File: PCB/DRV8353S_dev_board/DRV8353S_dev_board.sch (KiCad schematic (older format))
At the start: 136 parts

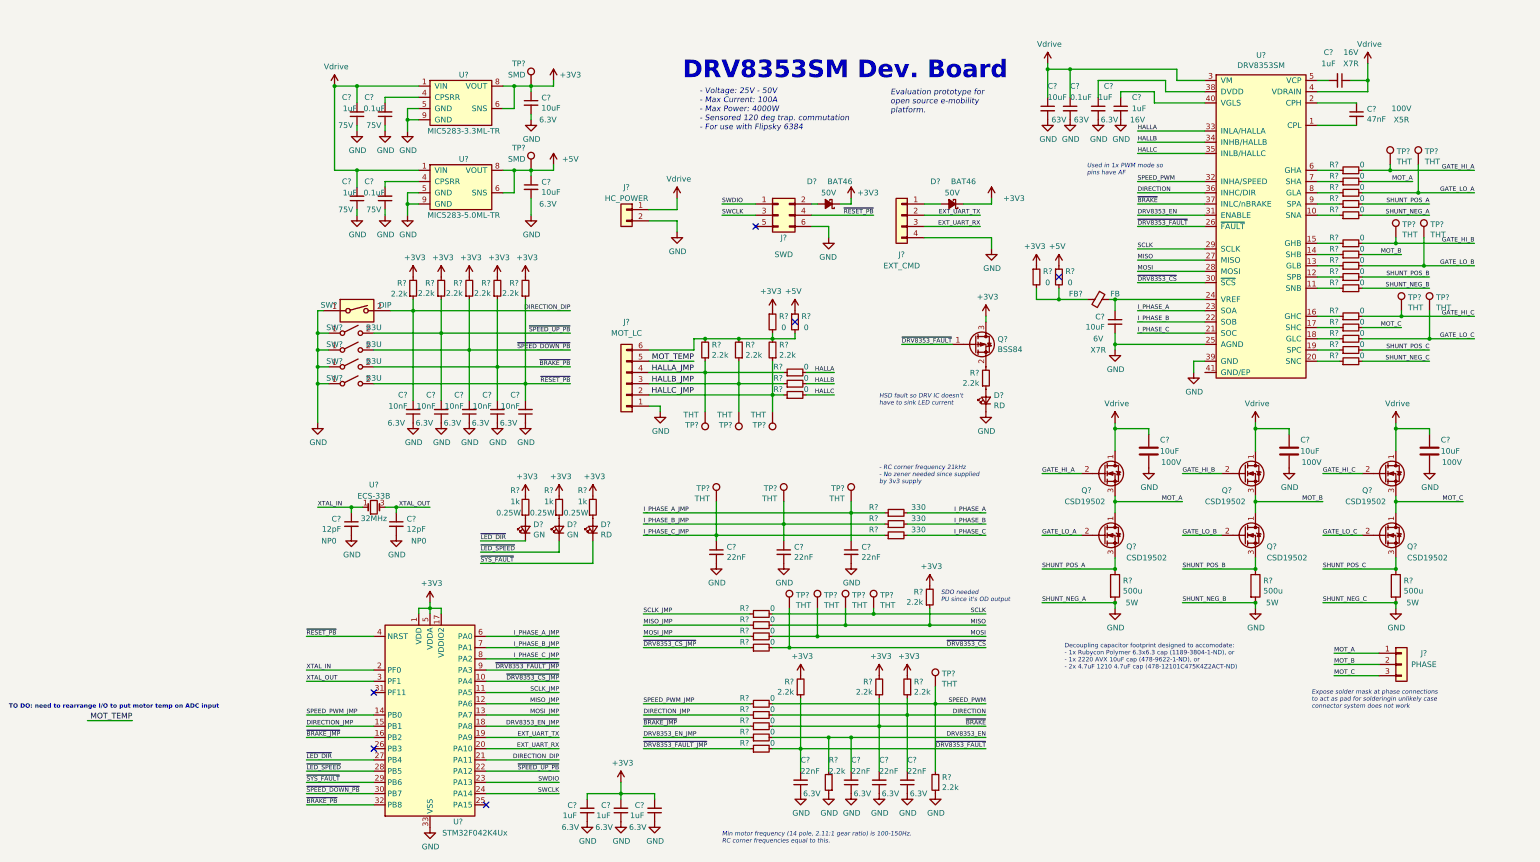
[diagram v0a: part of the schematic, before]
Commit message: High Current Routing planning
Planning how the high current routing will work with the gate drive signals
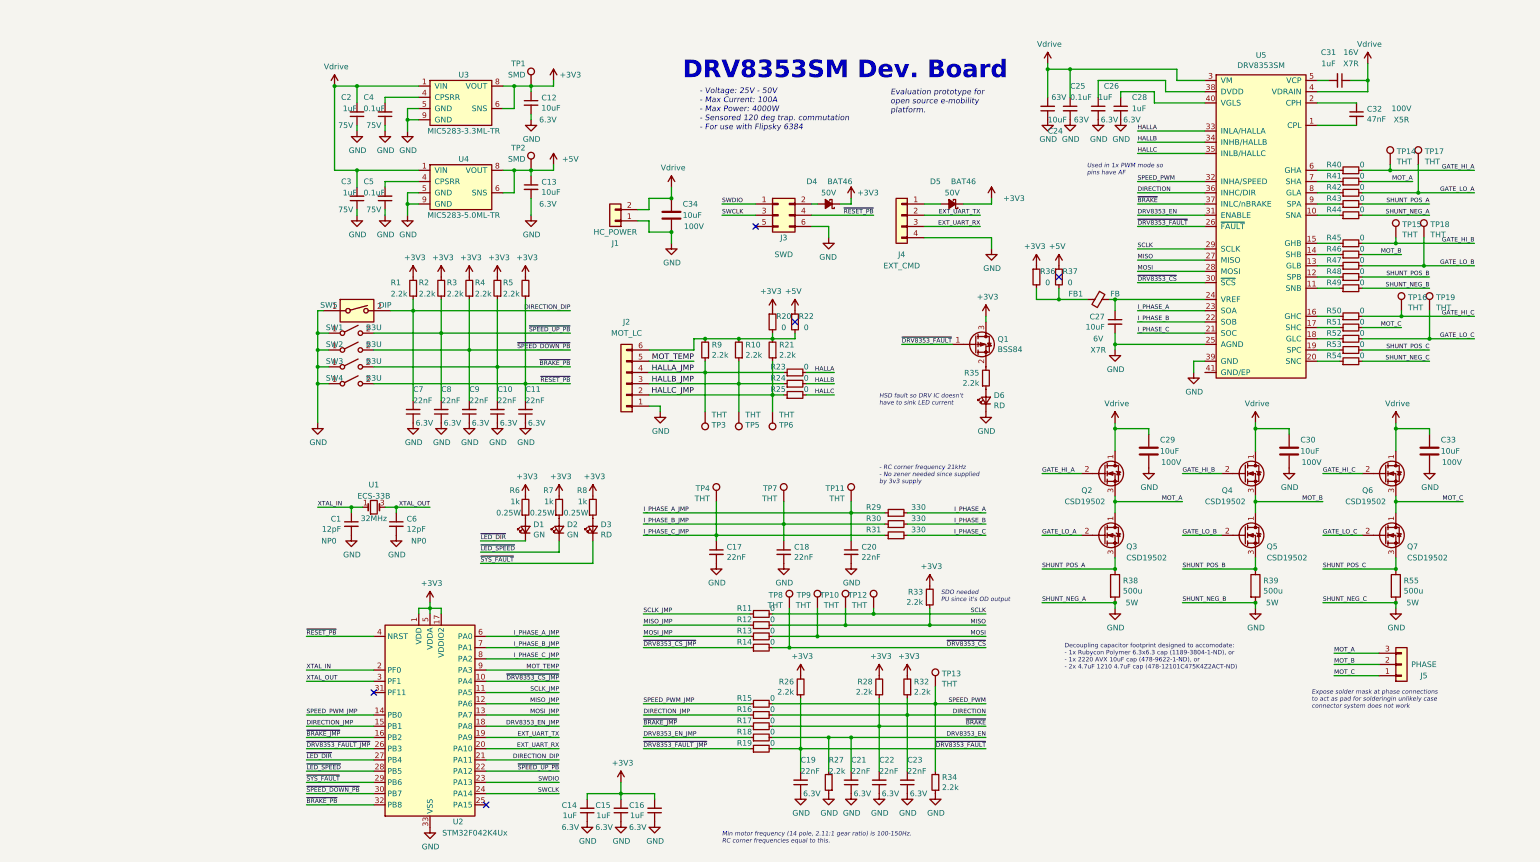
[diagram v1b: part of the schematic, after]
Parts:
- removed C? (x2): 1uF, symbol Device:C_Small
- removed C? (x5): 10nF, symbol Device:C_Small
- removed C? (x2): 1uF, Capacitor_SMD:C_0603_1608Metric, symbol Device:C_Small
- removed R? (x5): 2.2k, symbol Device:R_Small
- removed TP? (x16): THT, TestPoint:TestPoint_Keystone_5000-5004_Miniature, symbol Connector:TestPoint
- added C10, C11, C7, C8, C9: 22nF, Capacitor_SMD:C_0603_1608Metric, symbol Device:C_Small
- added C15, C16, C28, C3: 1uF, Capacitor_SMD:C_0805_2012Metric, symbol Device:C_Small
- added C34: 10uF, DRV8353S_dev_board:bridge_caps, symbol Device:C
- added R1, R2, R3, R4, R5: 2.2k, Resistor_SMD:R_0603_1608Metric, symbol Device:R_Small
- added TP10, TP11, TP12, TP13, TP14, TP15, TP16, TP17, TP18, TP19, TP3, TP5, TP6, TP7, TP8, TP9: THT, DRV8353S_dev_board:keystone_5001, symbol Connector:TestPoint
- C1, C6: renamed from C?; footprint (none) -> Capacitor_SMD:C_0603_1608Metric; Digikey (none) -> 478-10188-1-ND
- C12, C13, C24, C27: renamed from C?; footprint (none) -> Capacitor_SMD:C_1210_3225Metric; Digikey (none) -> 445-181609-1-ND
- C14: renamed from C?; footprint Capacitor_SMD:C_0603_1608Metric -> Capacitor_SMD:C_0805_2012Metric; Digikey (none) -> 478-12143-1-ND
- C17, C18, C19, C20, C21, C22, C23: renamed from C?; Digikey (none) -> 445-5663-1-ND
- C2, C26, C31: renamed from C?; footprint (none) -> Capacitor_SMD:C_0805_2012Metric; Digikey (none) -> 478-12143-1-ND
- C25, C4, C5: renamed from C?; footprint (none) -> Capacitor_SMD:C_0805_2012Metric; Digikey (none) -> 1276-6840-1-ND
- C32: renamed from C?; footprint (none) -> Capacitor_SMD:C_0603_1608Metric; Digikey (none) -> 311-4050-1-ND
- TP4: renamed from TP?; footprint TestPoint:TestPoint_Keystone_5000-5004_Miniature -> DRV8353S_dev_board:keystone_5001
- gave numbers to parts that had none: 84
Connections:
- net +3V3: now also C15.2, C16.2, R1.2, R2.2, R3.2, R4.2, R5.2
- net DIRECTION_DIP: now also C7.2, R1.1
- net GATE_HI_A: now also TP14.1
- net GATE_HI_B: now also TP15.1
- net GATE_HI_C: now also TP16.1
- net GATE_LO_A: now also TP17.1
- net GATE_LO_B: now also TP18.1
- net GATE_LO_C: now also TP19.1
- net GND: now also C24.1, J1.1 (Pin_1), C10.1, C11.1, C15.1, C16.1, C28.2, C3.1, C34.2, C7.1, C8.1, C9.1; no longer C24.2, J1.2 (Pin_2)
- net HALLA_JMP: now also TP3.1
- net HALLB_JMP: now also TP5.1
- net HALLC_JMP: now also TP6.1
- net I_PHASE_A_JMP: now also TP11.1
- net I_PHASE_B_JMP: now also TP7.1
- net MISO: now also TP10.1
- net MOSI: now also TP9.1
- net MOT_A: now also J5.3 (Pin_3); no longer J5.1 (Pin_1)
- net MOT_C: now also J5.1 (Pin_1); no longer J5.3 (Pin_3)
- net MOT_TEMP: now also U2.9 (PA3)
- net SCLK: now also TP12.1
- net SPEED_PWM: now also TP13.1
- net Vdrive: now also C24.2, J1.2 (Pin_2), C3.2, C34.1; no longer C24.1, J1.1 (Pin_1)
- net ~BRAKE_PB: now also C10.2, R4.1
- net ~DRV8353_CS: now also TP8.1
- net ~DRV8353_FAULT_JMP: now also U2.26 (PB3); no longer U2.9 (PA3)
- net ~RESET_PB: now also C11.2, R5.1
- net ~SPEED_DOWN_PB: now also C9.2, R3.1
- net ~SPEED_UP_PB: now also C8.2, R2.1
- net at U5.40 (VGLS): now also C28.1
- no-connect marks 6 -> 5
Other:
- note removed: "TO DO: need to rearrange I/O to put motor temp on ADC input"
- moved on the sheet: J1

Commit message: more routing work
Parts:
- added C35: 22nF, Capacitor_SMD:C_0603_1608Metric, symbol Device:C_Small
- added R56: 330, Resistor_SMD:R_0603_1608Metric, symbol Device:R_Small
- added TP20: THT, DRV8353S_dev_board:keystone_5001, symbol Connector:TestPoint
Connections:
- net GND: now also C35.2
- net HALLA: now also R9.1, TP3.1
- net HALLA_JMP: no longer R9.1, TP3.1
- net HALLB: now also R10.1, TP5.1
- net HALLB_JMP: no longer R10.1, TP5.1
- net HALLC: now also R21.1, TP6.1
- net HALLC_JMP: no longer R21.1, TP6.1
- net I_PHASE_A_JMP: now also U2.9 (PA3); no longer U2.6 (PA0)
- net I_PHASE_B_JMP: now also U2.8 (PA2); no longer U2.7 (PA1)
- net I_PHASE_C_JMP: now also U2.7 (PA1); no longer U2.8 (PA2)
- net MOT_TEMP: now also R56.2; no longer U2.9 (PA3)
- new net MOT_TEMP_JMP: C35.1, R56.1, TP20.1, U2.6 (PA0)
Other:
- moved on the sheet: C17, C18, C20, R10, R20, R21, R22, R23, R24, R25, R29, R30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

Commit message: Final (?) layout
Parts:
- removed R36, R37: 0, Resistor_SMD:R_0603_1608Metric, symbol Device:R_Small
- C1, C10, C11, C12, C13, C14, C15, C16, C17, C18, C19, C2, C20, C21, C22, C23, C24, C25, C26, C27, C28, C3, C31, C32, C35, C4, C5, C6, C7, C8, C9: symbol Device:C_Small -> DRV8353S_dev_board-rescue:C_Small-Device
- C29, C30, C33, C34: symbol Device:C -> DRV8353S_dev_board-rescue:C-Device
- D1, D2, D3, D6: symbol Device:LED_Small -> DRV8353S_dev_board-rescue:LED_Small-Device
- D4, D5: symbol Device:D_Schottky_Small_ALT -> DRV8353S_dev_board-rescue:D_Schottky_Small_ALT-Device
- FB1: symbol Device:Ferrite_Bead_Small -> DRV8353S_dev_board-rescue:Ferrite_Bead_Small-Device
- J1: symbol Connector_Generic:Conn_01x02 -> DRV8353S_dev_board-rescue:Conn_01x02-Connector_Generic
- J2: symbol Connector_Generic:Conn_01x06 -> DRV8353S_dev_board-rescue:Conn_01x06-Connector_Generic
- J3: symbol Connector_Generic:Conn_02x03_Odd_Even -> DRV8353S_dev_board-rescue:Conn_02x03_Odd_Even-Connector_Generic
- J4: symbol Connector_Generic:Conn_01x04 -> DRV8353S_dev_board-rescue:Conn_01x04-Connector_Generic
- J5: symbol Connector_Generic:Conn_01x03 -> DRV8353S_dev_board-rescue:Conn_01x03-Connector_Generic
- Q1: symbol Device:Q_PMOS_GSD -> DRV8353S_dev_board-rescue:Q_PMOS_GSD-Device
- Q2, Q3, Q4, Q5, Q6, Q7: symbol Device:Q_NMOS_DGS -> DRV8353S_dev_board-rescue:Q_NMOS_DGS-Device
- R1, R10, R11, R12, R13, R14, R15, R16, R17, R18, R19, R2, R20, R21, R22, R23, R24, R25, R26, R27, R28, R29, R3, R30, R31, R32, R33, R34, R35, R4, R40, R41, R42, R43, R44, R45, R46, R47, R48, R49, R5, R50, R51, R52, R53, R54, R56, R6, R7, R8, R9: symbol Device:R_Small -> DRV8353S_dev_board-rescue:R_Small-Device
- R38, R39, R55: symbol Device:R -> DRV8353S_dev_board-rescue:R-Device
- SW1, SW2, SW3, SW4: symbol Switch:SW_SPST -> DRV8353S_dev_board-rescue:SW_SPST-Switch
- SW5: symbol Switch:SW_DIP_x01 -> DRV8353S_dev_board-rescue:SW_DIP_x01-Switch
- TP1, TP10, TP11, TP12, TP13, TP14, TP15, TP16, TP17, TP18, TP19, TP2, TP20, TP3, TP4, TP5, TP6, TP7, TP8, TP9: symbol Connector:TestPoint -> DRV8353S_dev_board-rescue:TestPoint-Connector
- U2: symbol MCU_ST_STM32F0:STM32F042K4Ux -> DRV8353S_dev_board-rescue:STM32F042K4Ux-MCU_ST_STM32F0
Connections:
- net DIRECTION_DIP: now also U2.29 (PB6); no longer U2.21 (PA11)
- net DIRECTION_JMP: now also U2.16 (PB2); no longer U2.15 (PB1)
- net DRV8353_EN_JMP: now also U2.15 (PB1); no longer U2.18 (PA8)
- net GND: now also J3.2 (Pin_2), U5.41 (GND/EP); no longer J3.6 (Pin_6)
- net I_PHASE_A_JMP: now also U2.8 (PA2); no longer U2.9 (PA3)
- net I_PHASE_B_JMP: now also U2.7 (PA1); no longer U2.8 (PA2)
- net I_PHASE_C_JMP: now also U2.6 (PA0); no longer U2.7 (PA1)
- net MOT_TEMP: now also TP20.1
- net MOT_TEMP_JMP: now also U2.9 (PA3); no longer TP20.1, U2.6 (PA0)
- net SPEED_PWM_JMP: now also U2.32 (PB8); no longer U2.14 (PB0)
- net ~BRAKE_JMP: now also U2.18 (PA8); no longer U2.16 (PB2)
- net ~BRAKE_PB: now also U2.26 (PB3); no longer U2.32 (PB8)
- net ~DRV8353_FAULT_JMP: now also U2.14 (PB0); no longer U2.26 (PB3)
- net ~LED_DIR: now also U2.25 (PA15); no longer U2.27 (PB4)
- net ~LED_SPEED: now also U2.22 (PA12); no longer U2.28 (PB5)
- net ~RESET_PB: now also J3.6 (Pin_6); no longer J3.4 (Pin_4)
- net ~SPEED_DOWN_PB: now also U2.27 (PB4); no longer U2.30 (PB7)
- net ~SPEED_UP_PB: now also U2.28 (PB5); no longer U2.22 (PA12)
- net ~SYS_FAULT: now also U2.21 (PA11); no longer U2.29 (PB6)
- net at D4.2 (A): now also J3.5 (Pin_5); no longer J3.2 (Pin_2)
- no-connect marks 5 -> 4
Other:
- moved on the sheet: C14, C15, C16, TP20

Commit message: Final Routing
Moved around encoder stuff. Also added decoupling capacitor near encoder connector.
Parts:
- added C36: 22nF, Capacitor_SMD:C_0603_1608Metric, symbol DRV8353S_dev_board-rescue:C_Small-Device
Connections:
- net GND: now also C36.2
- net HALLA: no longer R9.1
- net HALLA_JMP: now also R9.1
- net HALLB: no longer R10.1
- net HALLB_JMP: now also R10.1
- net HALLC: no longer R21.1
- net HALLC_JMP: now also R21.1
- net at J2.6 (Pin_6), R10.2, R20.2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: now also C36.1
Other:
- moved on the sheet: J2, R10, R20, R21, R22, R23, R24, R25, R9, TP3, TP5, TP6

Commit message: Most DRV routing done.
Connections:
- net I_PHASE_A: now also TP11.1
- net I_PHASE_A_JMP: no longer TP11.1
- net I_PHASE_B: now also TP7.1
- net I_PHASE_B_JMP: no longer TP7.1
- net I_PHASE_C: now also TP4.1
- net I_PHASE_C_JMP: no longer TP4.1
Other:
- moved on the sheet: R29, R30, R31, R56, TP11, TP20, TP4, TP7
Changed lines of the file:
@@
 	1    0    0    -1
 $EndComp
-Text Notes 5200 4450 0    39   Italic 0
+Text Notes 4350 4400 0    39   Italic 0
 - RC corner frequency 21kHz \n- No zener needed since supplied\nby 3v3 supply
 $Comp
 L DRV8353S_dev_board-rescue:R_Small-Device R56
 U 1 1 6071FAF6
-P 5950 4550
-F 0 "R56" V 6000 4750 50  0000 C CNN
-F 1 "330" V 6000 4350 50  0000 C CNN
-F 2 "Resistor_SMD:R_0603_1608Metric" H 5950 4550 50  0001 C CNN
-F 3 "https://www.bourns.com/docs/product-datasheets/CRxxxxx.pdf" H 5950 4550 50  0001 C CNN
-F 4 "CR0603-JW-331ELFCT-ND" V 5950 4550 50  0001 C CNN "Digikey"
-	1    5950 4550
+P 5650 4550
+F 0 "R56" V 5700 4750 50  0000 C CNN
+F 1 "330" V 5700 4350 50  0000 C CNN
+F 2 "Resistor_SMD:R_0603_1608Metric" H 5650 4550 50  0001 C CNN
+F 3 "https://www.bourns.com/docs/product-datasheets/CRxxxxx.pdf" H 5650 4550 50  0001 C CNN
+F 4 "CR0603-JW-331ELFCT-ND" V 5650 4550 50  0001 C CNN "Digikey"
+	1    5650 4550
 	0    -1   -1   0
 $EndComp
@@
 L DRV8353S_dev_board-rescue:R_Small-Device R29
 U 1 1 6043F748
-P 5950 4650
-F 0 "R29" V 6000 4850 50  0000 C CNN
-F 1 "330" V 6000 4450 50  0000 C CNN
-F 2 "Resistor_SMD:R_0603_1608Metric" H 5950 4650 50  0001 C CNN
-F 3 "https://www.bourns.com/docs/product-datasheets/CRxxxxx.pdf" H 5950 4650 50  0001 C CNN
-F 4 "CR0603-JW-331ELFCT-ND" V 5950 4650 50  0001 C CNN "Digikey"
-	1    5950 4650
+P 5650 4650
+F 0 "R29" V 5700 4850 50  0000 C CNN
+F 1 "330" V 5700 4450 50  0000 C CNN
+F 2 "Resistor_SMD:R_0603_1608Metric" H 5650 4650 50  0001 C CNN
+F 3 "https://www.bourns.com/docs/product-datasheets/CRxxxxx.pdf" H 5650 4650 50  0001 C CNN
+F 4 "CR0603-JW-331ELFCT-ND" V 5650 4650 50  0001 C CNN "Digikey"
+	1    5650 4650
 	0    -1   -1   0
 $EndComp
 Wire Wire Line
-	6350 4550 6350 4450
+	6400 4550 6400 4450
 $Comp
 L DRV8353S_dev_board-rescue:TestPoint-Connector TP20
 U 1 1 608C7A2F
-P 6350 4450
-F 0 "TP20" H 6300 4750 50  0000 L CNN
-F 1 "THT" H 6300 4650 50  0000 L CNN
-F 2 "DRV8353S_dev_board:keystone_5001" H 6550 4450 50  0001 C CNN
-F 3 "https://www.keyelco.com/userAssets/file/M65p56.pdf" H 6550 4450 50  0001 C CNN
-F 4 "36-5001-ND" H 6350 4450 50  0001 C CNN "Digikey"
-	1    6350 4450
+P 6400 4450
+F 0 "TP20" H 6350 4750 50  0000 L CNN
+F 1 "THT" H 6350 4650 50  0000 L CNN
+F 2 "DRV8353S_dev_board:keystone_5001" H 6600 4450 50  0001 C CNN
+F 3 "https://www.keyelco.com/userAssets/file/M65p56.pdf" H 6600 4450 50  0001 C CNN
+F 4 "36-5001-ND" H 6400 4450 50  0001 C CNN "Digikey"
+	1    6400 4450
 	-1   0    0    -1
 $EndComp
@@
 L DRV8353S_dev_board-rescue:TestPoint-Connector TP11
 U 1 1 604F9F69
-P 5050 4450
-F 0 "TP11" H 5000 4750 50  0000 L CNN
-F 1 "THT" H 5000 4650 50  0000 L CNN
-F 2 "DRV8353S_dev_board:keystone_5001" H 5250 4450 50  0001 C CNN
-F 3 "https://www.keyelco.com/userAssets/file/M65p56.pdf" H 5250 4450 50  0001 C CNN
-F 4 "36-5001-ND" H 5050 4450 50  0001 C CNN "Digikey"
-	1    5050 4450
+P 6250 4450
+F 0 "TP11" H 6200 4750 50  0000 L CNN
+F 1 "THT" H 6200 4650 50  0000 L CNN
+F 2 "DRV8353S_dev_board:keystone_5001" H 6450 4450 50  0001 C CNN
+F 3 "https://www.keyelco.com/userAssets/file/M65p56.pdf" H 6450 4450 50  0001 C CNN
+F 4 "36-5001-ND" H 6250 4450 50  0001 C CNN "Digikey"
+	1    6250 4450
 	-1   0    0    -1
 $EndComp
@@
 L DRV8353S_dev_board-rescue:TestPoint-Connector TP7
 U 1 1 604F9342
-P 4700 4450
-F 0 "TP7" H 4650 4750 50  0000 L CNN
-F 1 "THT" H 4650 4650 50  0000 L CNN
-F 2 "DRV8353S_dev_board:keystone_5001" H 4900 4450 50  0001 C CNN
-F 3 "https://www.keyelco.com/userAssets/file/M65p56.pdf" H 4900 4450 50  0001 C CNN
-F 4 "36-5001-ND" H 4700 4450 50  0001 C CNN "Digikey"
-	1    4700 4450
+P 6100 4450
+F 0 "TP7" H 6050 4750 50  0000 L CNN
+F 1 "THT" H 6050 4650 50  0000 L CNN
+F 2 "DRV8353S_dev_board:keystone_5001" H 6300 4450 50  0001 C CNN
+F 3 "https://www.keyelco.com/userAssets/file/M65p56.pdf" H 6300 4450 50  0001 C CNN
+F 4 "36-5001-ND" H 6100 4450 50  0001 C CNN "Digikey"
+	1    6100 4450
 	-1   0    0    -1
 $EndComp
 Wire Wire Line
-	5050 4650 5050 4450
+	6250 4650 6250 4450
 Wire Wire Line
-	4700 4750 4700 4450
+	6100 4750 6100 4450
 $Comp
 L DRV8353S_dev_board-rescue:TestPoint-Connector TP4
 U 1 1 605697AB
-P 4350 4450
-F 0 "TP4" H 4300 4750 50  0000 L CNN
-F 1 "THT" H 4300 4650 50  0000 L CNN
-F 2 "DRV8353S_dev_board:keystone_5001" H 4550 4450 50  0001 C CNN
-F 3 "https://www.keyelco.com/userAssets/file/M65p56.pdf" H 4550 4450 50  0001 C CNN
-F 4 "36-5001-ND" H 4350 4450 50  0001 C CNN "Digikey"
-	1    4350 4450
+P 5950 4450
+F 0 "TP4" H 5900 4750 50  0000 L CNN
+F 1 "THT" H 5900 4650 50  0000 L CNN
+F 2 "DRV8353S_dev_board:keystone_5001" H 6150 4450 50  0001 C CNN
+F 3 "https://www.keyelco.com/userAssets/file/M65p56.pdf" H 6150 4450 50  0001 C CNN
+F 4 "36-5001-ND" H 5950 4450 50  0001 C CNN "Digikey"
+	1    5950 4450
 	-1   0    0    -1
 $EndComp
 Wire Wire Line
-	4350 4850 4350 4450
+	5950 4850 5950 4450
 Wire Wire Line
 	3700 4850 4350 4850
@@
 L DRV8353S_dev_board-rescue:R_Small-Device R31
 U 1 1 6051BAC6
-P 5950 4850
-F 0 "R31" V 6000 5050 50  0000 C CNN
-F 1 "330" V 6000 4650 50  0000 C CNN
-F 2 "Resistor_SMD:R_0603_1608Metric" H 5950 4850 50  0001 C CNN
-F 3 "https://www.bourns.com/docs/product-datasheets/CRxxxxx.pdf" H 5950 4850 50  0001 C CNN
-F 4 "CR0603-JW-331ELFCT-ND" V 5950 4850 50  0001 C CNN "Digikey"
-	1    5950 4850
+P 5650 4850
+F 0 "R31" V 5700 5050 50  0000 C CNN
+F 1 "330" V 5700 4650 50  0000 C CNN
+F 2 "Resistor_SMD:R_0603_1608Metric" H 5650 4850 50  0001 C CNN
+F 3 "https://www.bourns.com/docs/product-datasheets/CRxxxxx.pdf" H 5650 4850 50  0001 C CNN
+F 4 "CR0603-JW-331ELFCT-ND" V 5650 4850 50  0001 C CNN "Digikey"
+	1    5650 4850
 	0    -1   -1   0
 $EndComp
@@
 L DRV8353S_dev_board-rescue:R_Small-Device R30
 U 1 1 6051B911
-P 5950 4750
-F 0 "R30" V 6000 4950 50  0000 C CNN
-F 1 "330" V 6000 4550 50  0000 C CNN
-F 2 "Resistor_SMD:R_0603_1608Metric" H 5950 4750 50  0001 C CNN
-F 3 "https://www.bourns.com/docs/product-datasheets/CRxxxxx.pdf" H 5950 4750 50  0001 C CNN
-F 4 "CR0603-JW-331ELFCT-ND" V 5950 4750 50  0001 C CNN "Digikey"
-	1    5950 4750
+P 5650 4750
+F 0 "R30" V 5700 4950 50  0000 C CNN
+F 1 "330" V 5700 4550 50  0000 C CNN
+F 2 "Resistor_SMD:R_0603_1608Metric" H 5650 4750 50  0001 C CNN
+F 3 "https://www.bourns.com/docs/product-datasheets/CRxxxxx.pdf" H 5650 4750 50  0001 C CNN
+F 4 "CR0603-JW-331ELFCT-ND" V 5650 4750 50  0001 C CNN "Digikey"
+	1    5650 4750
 	0    -1   -1   0
 $EndComp
 Wire Wire Line
-	6050 4550 6350 4550
-Wire Wire Line
-	6050 4650 6750 4650
-Wire Wire Line
-	6050 4750 6750 4750
-Wire Wire Line
-	6050 4850 6750 4850
+	5750 4750 6100 4750
 Connection ~ 4350 4850
 Wire Wire Line
-	4350 4850 5850 4850
+	4350 4850 5550 4850
 Connection ~ 4700 4750
 Wire Wire Line
-	4700 4750 5850 4750
+	4700 4750 5550 4750
 Connection ~ 5050 4650
 Wire Wire Line
-	5050 4650 5850 4650
+	5050 4650 5550 4650
 Connection ~ 5450 4550
 Wire Wire Line
-	5450 4550 5850 4550
+	5450 4550 5550 4550
 Wire Wire Line
 	3700 4750 4700 4750
@@
 Wire Wire Line
 	3550 3600 4650 3600
-Connection ~ 6350 4550
-Wire Wire Line
-	6350 4550 6750 4550
 Connection ~ 4950 3400
 Wire Wire Line
@@
 Wire Wire Line
 	5150 3600 5350 3600
+Wire Wire Line
+	5750 4850 5950 4850
+Connection ~ 5950 4850
+Connection ~ 6100 4750
+Wire Wire Line
+	6100 4750 6750 4750
+Wire Wire Line
+	5950 4850 6750 4850
+Connection ~ 6400 4550
+Wire Wire Line
+	6400 4550 6750 4550
+Wire Wire Line
+	5750 4550 6400 4550
+Connection ~ 6250 4650
+Wire Wire Line
+	6250 4650 6750 4650
+Wire Wire Line
+	5750 4650 6250 4650
 $EndSCHEMATC

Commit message: Finished routing (?)
All signals routed. No DRC errors.
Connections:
- net +3V3: now also FB1.2
- net EXT_UART_RX: now also J4.2 (Pin_2); no longer J4.3 (Pin_3)
- net EXT_UART_TX: now also J4.3 (Pin_3); no longer J4.2 (Pin_2)
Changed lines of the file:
@@
 	5500 2050 5200 2050
-Wire Wire Line
-	6200 2050 6700 2050
 Wire Wire Line
 	6200 2150 6700 2150
 Text Label 6700 2150 2    39   ~ 0
-EXT_UART_RX
-Text Label 6700 2050 2    39   ~ 0
 EXT_UART_TX
 Text Label 650  5800 0    39   ~ 0
@@
 L DRV8353S_dev_board-rescue:+3V3-power #PWR?
 U 1 1 605681A5
-P 7400 2500
+P 7400 2700
 AR Path="/60313041/605681A5" Ref="#PWR?"  Part="1"
 AR Path="/605681A5" Ref="#PWR0149"  Part="1"
-F 0 "#PWR0149" H 7400 2350 50  0001 C CNN
-F 1 "+3V3" H 7415 2673 50  0000 C CNN
-F 2 "" H 7400 2500 50  0001 C CNN
-F 3 "" H 7400 2500 50  0001 C CNN
-	1    7400 2500
+F 0 "#PWR0149" H 7400 2550 50  0001 C CNN
+F 1 "+3V3" H 7415 2873 50  0000 C CNN
+F 2 "" H 7400 2700 50  0001 C CNN
+F 3 "" H 7400 2700 50  0001 C CNN
+	1    7400 2700
 	-1   0    0    -1
 $EndComp
-Connection ~ 7400 2800
-Wire Wire Line
-	7200 2800 7400 2800
 Wire Wire Line
 	650  7100 1300 7100
@@
 Wire Wire Line
 	5750 4650 6250 4650
+Text Label 6700 2050 2    39   ~ 0
+EXT_UART_RX
+Wire Wire Line
+	6200 2050 6700 2050
 $EndSCHEMATC
